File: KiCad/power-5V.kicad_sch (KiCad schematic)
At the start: 8 parts, among them U1 TPSM63606RDLR

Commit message: feat(pcb): add output capacitors
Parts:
- added C5, C6: (no value), symbol GCM32ER70J476KE19L:GCM32ER70J476KE19L
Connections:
- net GNDREF: now also C5.1, C6.1
- net VCC5: now also C5.2, C6.2
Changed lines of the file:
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@@
   (junction (at 116.84 83.82) (diameter 0) (color 0 0 0 0)
   )
-  (junction (at 177.8 111.76) (diameter 0) (color 0 0 0 0)
+  (junction (at 195.58 129.54) (diameter 0) (color 0 0 0 0)
+  )
+  (junction (at 185.42 111.76) (diameter 0) (color 0 0 0 0)
   )
   (junction (at 104.14 129.54) (diameter 0) (color 0 0 0 0)
@@
   (junction (at 128.27 129.54) (diameter 0) (color 0 0 0 0)
   )
+  (junction (at 219.71 129.54) (diameter 0) (color 0 0 0 0)
+  )
   (junction (at 177.8 129.54) (diameter 0) (color 0 0 0 0)
   )
@@
   (junction (at 180.34 83.82) (diameter 0) (color 0 0 0 0)
   )
+  (junction (at 219.71 83.82) (diameter 0) (color 0 0 0 0)
+  )
   (junction (at 195.58 107.95) (diameter 0) (color 0 0 0 0)
   )
@@
   (junction (at 177.8 121.92) (diameter 0) (color 0 0 0 0)
   )
+  (junction (at 232.41 83.82) (diameter 0) (color 0 0 0 0)
+  )
+  (no_connect (at 177.8 104.14))
   (no_connect (at 134.62 121.92))
   (no_connect (at 134.62 106.68))
   (no_connect (at 134.62 111.76))
-  (no_connect (at 177.8 104.14))
   (wire (pts (xy 104.14 81.28) (xy 104.14 83.82))
     (stroke (width 0) (type default) (color 0 0 0 0))
@@
     (stroke (width 0) (type default) (color 0 0 0 0))
   )
-  (wire (pts (xy 177.8 111.76) (xy 181.61 111.76))
-    (stroke (width 0) (type default) (color 0 0 0 0))
-  )
   (wire (pts (xy 207.01 107.95) (xy 195.58 107.95))
     (stroke (width 0) (type default) (color 0 0 0 0))
@@
     (stroke (width 0) (type default) (color 0 0 0 0))
   )
+  (wire (pts (xy 219.71 88.9) (xy 219.71 83.82))
+    (stroke (width 0) (type default) (color 0 0 0 0))
+  )
   (wire (pts (xy 177.8 81.28) (xy 180.34 81.28))
     (stroke (width 0) (type default) (color 0 0 0 0))
@@
     (stroke (width 0) (type default) (color 0 0 0 0))
   )
-  (wire (pts (xy 177.8 109.22) (xy 177.8 111.76))
-    (stroke (width 0) (type default) (color 0 0 0 0))
-  )
   (wire (pts (xy 186.69 105.41) (xy 195.58 105.41))
     (stroke (width 0) (type default) (color 0 0 0 0))
@@
     (stroke (width 0) (type default) (color 0 0 0 0))
   )
+  (wire (pts (xy 185.42 109.22) (xy 185.42 111.76))
+    (stroke (width 0) (type default) (color 0 0 0 0))
+  )
   (wire (pts (xy 180.34 81.28) (xy 180.34 83.82))
     (stroke (width 0) (type default) (color 0 0 0 0))
@@
     (stroke (width 0) (type default) (color 0 0 0 0))
   )
+  (wire (pts (xy 185.42 111.76) (xy 185.42 115.57))
+    (stroke (width 0) (type default) (color 0 0 0 0))
+  )
   (wire (pts (xy 207.01 83.82) (xy 207.01 88.9))
     (stroke (width 0) (type default) (color 0 0 0 0))
   )
+  (wire (pts (xy 232.41 88.9) (xy 232.41 83.82))
+    (stroke (width 0) (type default) (color 0 0 0 0))
+  )
   (wire (pts (xy 116.84 83.82) (xy 116.84 86.36))
     (stroke (width 0) (type default) (color 0 0 0 0))
@@
     (stroke (width 0) (type default) (color 0 0 0 0))
   )
+  (wire (pts (xy 177.8 109.22) (xy 185.42 109.22))
+    (stroke (width 0) (type default) (color 0 0 0 0))
+  )
+  (wire (pts (xy 232.41 101.6) (xy 232.41 129.54))
+    (stroke (width 0) (type default) (color 0 0 0 0))
+  )
   (wire (pts (xy 195.58 105.41) (xy 195.58 107.95))
     (stroke (width 0) (type default) (color 0 0 0 0))
   )
+  (wire (pts (xy 219.71 101.6) (xy 219.71 129.54))
+    (stroke (width 0) (type default) (color 0 0 0 0))
+  )
   (wire (pts (xy 177.8 119.38) (xy 177.8 121.92))
     (stroke (width 0) (type default) (color 0 0 0 0))
@@
     (stroke (width 0) (type default) (color 0 0 0 0))
   )
+  (wire (pts (xy 219.71 83.82) (xy 232.41 83.82))
+    (stroke (width 0) (type default) (color 0 0 0 0))
+  )
   (wire (pts (xy 129.54 101.6) (xy 119.38 101.6))
     (stroke (width 0) (type default) (color 0 0 0 0))
@@
     (stroke (width 0) (type default) (color 0 0 0 0))
   )
+  (wire (pts (xy 232.41 83.82) (xy 237.49 83.82))
+    (stroke (width 0) (type default) (color 0 0 0 0))
+  )
   (wire (pts (xy 129.54 101.6) (xy 129.54 67.31))
     (stroke (width 0) (type default) (color 0 0 0 0))
@@
     (stroke (width 0) (type default) (color 0 0 0 0))
   )
-  (wire (pts (xy 207.01 83.82) (xy 220.98 83.82))
+  (wire (pts (xy 207.01 83.82) (xy 219.71 83.82))
     (stroke (width 0) (type default) (color 0 0 0 0))
   )
@@
     (stroke (width 0) (type default) (color 0 0 0 0))
   )
+  (wire (pts (xy 177.8 111.76) (xy 185.42 111.76))
+    (stroke (width 0) (type default) (color 0 0 0 0))
+  )
+  (wire (pts (xy 232.41 129.54) (xy 219.71 129.54))
+    (stroke (width 0) (type default) (color 0 0 0 0))
+  )
+  (wire (pts (xy 219.71 129.54) (xy 195.58 129.54))
+    (stroke (width 0) (type default) (color 0 0 0 0))
+  )
   (wire (pts (xy 119.38 127) (xy 119.38 129.54))
     (stroke (width 0) (type default) (color 0 0 0 0))
@@
     (stroke (width 0) (type default) (color 0 0 0 0))
   )
-  (global_label "VCC5" (shape output) (at 220.98 83.82 0) (fields_autoplaced)
+  (global_label "VCC5" (shape output) (at 237.49 83.82 0) (fields_autoplaced)
     (effects (font (size 1.27 1.27)) (justify left))
-    (property "Intersheet References" "${INTERSHEET_REFS}" (id 0) (at 228.2312 83.7406 0)
+    (property "Intersheet References" "${INTERSHEET_REFS}" (id 0) (at 244.7412 83.7406 0)
       (effects (font (size 1.27 1.27)) (justify left) hide)
     )
@@
     (pin "2")
   )
+  (symbol (lib_id "GCM32ER70J476KE19L:GCM32ER70J476KE19L") (at 232.41 101.6 90) (unit 1)
+    (in_bom yes) (on_board yes) (fields_autoplaced)
+    (property "Reference" "C6" (id 0) (at 236.22 93.9799 90)
+      (effects (font (size 1.27 1.27)) (justify right))
+    )
+    (property "Value" "" (id 1) (at 236.22 96.5199 90)
+      (effects (font (size 1.27 1.27)) (justify right))
+    )
+    (property "Footprint" "" (id 2) (at 231.14 92.71 0)
+      (effects (font (size 1.27 1.27)) (justify left) hide)
+    )
+    (property "Datasheet" "" (id 3) (at 233.68 92.71 0)
+      (effects (font (size 1.27 1.27)) (justify left) hide)
+    )
+    (property "Description" "Chip Multilayer Ceramic Capacitors for Automotive" (id 4) (at 236.22 92.71 0)
+      (effects (font (size 1.27 1.27)) (justify left) hide)
+    )
+    (property "Height" "2.7" (id 5) (at 238.76 92.71 0)
+      (effects (font (size 1.27 1.27)) (justify left) hide)
+    )
+    (property "Mouser Part Number" "81-GCM32ER70J476KE9L" (id 6) (at 241.3 92.71 0)
+      (effects (font (size 1.27 1.27)) (justify left) hide)
+    )
+    (property "Mouser Price/Stock" "https://www.mouser.co.uk/ProductDetail/Murata-Electronics/GCM32ER70J476KE19L?qs=pIXLFAqUTcbyFoZMTWAW5w%3D%3D" (id 7) (at 243.84 92.71 0)
+      (effects (font (size 1.27 1.27)) (justify left) hide)
+    )
+    (property "Manufacturer_Name" "Murata Electronics" (id 8) (at 246.38 92.71 0)
+      (effects (font (size 1.27 1.27)) (justify left) hide)
+    )
+    (property "Manufacturer_Part_Number" "GCM32ER70J476KE19L" (id 9) (at 248.92 92.71 0)
+      (effects (font (size 1.27 1.27)) (justify left) hide)
+    )
+    (pin "1")
+    (pin "2")
+  )
   (symbol (lib_id "CRCW040210K0FKED:CRCW040210K0FKED") (at 195.58 127 90) (unit 1)
     (in_bom yes) (on_board yes) (fields_autoplaced)
@@
     (pin "1")
   )
-  (symbol (lib_id "power:GND") (at 181.61 111.76 90) (unit 1)
-    (in_bom yes) (on_board yes) (fields_autoplaced)
-    (property "Reference" "#PWR0104" (id 0) (at 187.96 111.76 0)
-      (effects (font (size 1.27 1.27)) hide)
-    )
-    (property "Value" "" (id 1) (at 185.42 111.7599 90)
-      (effects (font (size 1.27 1.27)) (justify right))
-    )
-    (property "Footprint" "" (id 2) (at 181.61 111.76 0)
-      (effects (font (size 1.27 1.27)) hide)
-    )
-    (property "Datasheet" "" (id 3) (at 181.61 111.76 0)
+  (symbol (lib_id "power:GND") (at 185.42 115.57 0) (unit 1)
+    (in_bom yes) (on_board yes) (fields_autoplaced)
+    (property "Reference" "#PWR0104" (id 0) (at 185.42 121.92 0)
+      (effects (font (size 1.27 1.27)) hide)
+    )
+    (property "Value" "" (id 1) (at 185.42 120.65 0))
+    (property "Footprint" "" (id 2) (at 185.42 115.57 0)
+      (effects (font (size 1.27 1.27)) hide)
+    )
+    (property "Datasheet" "" (id 3) (at 185.42 115.57 0)
       (effects (font (size 1.27 1.27)) hide)
     )
@@
       (effects (font (size 1.27 1.27)) (justify left) hide)
     )
+    (pin "1")
+    (pin "2")
+  )
+  (symbol (lib_id "GCM32ER70J476KE19L:GCM32ER70J476KE19L") (at 219.71 101.6 90) (unit 1)
+    (in_bom yes) (on_board yes) (fields_autoplaced)
+    (property "Reference" "C5" (id 0) (at 223.52 93.9799 90)
+      (effects (font (size 1.27 1.27)) (justify right))
+    )
+    (property "Value" "" (id 1) (at 223.52 96.5199 90)
+      (effects (font (size 1.27 1.27)) (justify right))
+    )
+    (property "Footprint" "" (id 2) (at 218.44 92.71 0)
+      (effects (font (size 1.27 1.27)) (justify left) hide)
+    )
+    (property "Datasheet" "" (id 3) (at 220.98 92.71 0)
+      (effects (font (size 1.27 1.27)) (justify left) hide)
+    )
+    (property "Description" "Chip Multilayer Ceramic Capacitors for Automotive" (id 4) (at 223.52 92.71 0)
+      (effects (font (size 1.27 1.27)) (justify left) hide)
+    )
+    (property "Height" "2.7" (id 5) (at 226.06 92.71 0)
+      (effects (font (size 1.27 1.27)) (justify left) hide)
+    )
+    (property "Mouser Part Number" "81-GCM32ER70J476KE9L" (id 6) (at 228.6 92.71 0)
+      (effects (font (size 1.27 1.27)) (justify left) hide)
+    )
+    (property "Mouser Price/Stock" "https://www.mouser.co.uk/ProductDetail/Murata-Electronics/GCM32ER70J476KE19L?qs=pIXLFAqUTcbyFoZMTWAW5w%3D%3D" (id 7) (at 231.14 92.71 0)
+      (effects (font (size 1.27 1.27)) (justify left) hide)
+    )
+    (property "Manufacturer_Name" "Murata Electronics" (id 8) (at 233.68 92.71 0)
+      (effects (font (size 1.27 1.27)) (justify left) hide)
+    )
+    (property "Manufacturer_Part_Number" "GCM32ER70J476KE19L" (id 9) (at 236.22 92.71 0)
+      (effects (font (size 1.27 1.27)) (justify left) hide)
+    )

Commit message: feat(pcb): add footprints
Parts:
- C1, C2: value (none) -> 10uF
- C3: value (none) -> 1uF
- C4: value (none) -> 8.2pF
- C5, C6: value (none) -> 47uF
- R1: value (none) -> 12.1k; footprint (none) -> Resistor_SMD:R_0402_1005Metric
- R2: value (none) -> 40.2k
- R3: value (none) -> 10k
- U1: footprint RDL0020A-MFG -> (none)
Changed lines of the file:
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@@
       (effects (font (size 1.27 1.27)) (justify left))
     )
-    (property "Value" "" (id 1) (at 130.81 124.4599 0)
+    (property "Value" "12.1k" (id 1) (at 130.81 124.4599 0)
       (effects (font (size 1.27 1.27)) (justify left))
     )
-    (property "Footprint" "" (id 2) (at 126.492 123.19 90)
+    (property "Footprint" "Resistor_SMD:R_0402_1005Metric" (id 2) (at 126.492 123.19 90)
       (effects (font (size 1.27 1.27)) hide)
     )
@@
       (effects (font (size 1.27 1.27)) hide)
     )
-    (property "Value" "" (id 1) (at 104.14 135.89 0))
+    (property "Value" "GNDREF" (id 1) (at 104.14 135.89 0))
     (property "Footprint" "" (id 2) (at 104.14 130.81 0)
       (effects (font (size 1.27 1.27)) hide)
@@
       (effects (font (size 1.27 1.27)) (justify right))
     )
-    (property "Value" "" (id 1) (at 120.65 93.9799 90)
+    (property "Value" "10uF" (id 1) (at 120.65 93.9799 90)
       (effects (font (size 1.27 1.27)) (justify right))
     )
@@
       (effects (font (size 1.27 1.27)) (justify right))
     )
-    (property "Value" "" (id 1) (at 123.19 121.9199 90)
+    (property "Value" "1uF" (id 1) (at 123.19 121.9199 90)
       (effects (font (size 1.27 1.27)) (justify right))
     )
@@
       (effects (font (size 1.27 1.27)) (justify right))
     )
-    (property "Value" "" (id 1) (at 236.22 96.5199 90)
+    (property "Value" "47uF" (id 1) (at 236.22 96.5199 90)
       (effects (font (size 1.27 1.27)) (justify right))
     )
@@
       (effects (font (size 1.27 1.27)) (justify right))
     )
-    (property "Value" "" (id 1) (at 198.12 119.3799 90)
+    (property "Value" "10k" (id 1) (at 198.12 119.3799 90)
       (effects (font (size 1.27 1.27)) (justify right))
     )
@@
       (effects (font (size 1.27 1.27)) (justify right))
     )
-    (property "Value" "" (id 1) (at 210.82 96.5199 90)
+    (property "Value" "8.2pF" (id 1) (at 210.82 96.5199 90)
       (effects (font (size 1.27 1.27)) (justify right))
     )
@@
       (effects (font (size 1.27 1.27)) (justify right))
     )
-    (property "Value" "" (id 1) (at 198.12 96.5199 90)
+    (property "Value" "40.2k" (id 1) (at 198.12 96.5199 90)
       (effects (font (size 1.27 1.27)) (justify right))
     )
@@
       (effects (font (size 1.27 1.27)) hide)
     )
-    (property "Value" "" (id 1) (at 104.14 76.2 0))
+    (property "Value" "+BATT" (id 1) (at 104.14 76.2 0))
     (property "Footprint" "" (id 2) (at 104.14 81.28 0)
       (effects (font (size 1.27 1.27)) hide)
@@
       (effects (font (size 1.27 1.27)) hide)
     )
-    (property "Value" "" (id 1) (at 185.42 120.65 0))
+    (property "Value" "GND" (id 1) (at 185.42 120.65 0))
     (property "Footprint" "" (id 2) (at 185.42 115.57 0)
       (effects (font (size 1.27 1.27)) hide)
@@
       (effects (font (size 1.524 1.524)))
     )
-    (property "Footprint" "RDL0020A-MFG" (id 2) (at 134.62 82.804 0)
+    (property "Footprint" "" (id 2) (at 134.62 82.804 0)
       (effects (font (size 1.524 1.524)) hide)
     )
@@
       (effects (font (size 1.27 1.27)) (justify right))
     )
-    (property "Value" "" (id 1) (at 107.95 93.9799 90)
+    (property "Value" "10uF" (id 1) (at 107.95 93.9799 90)
       (effects (font (size 1.27 1.27)) (justify right))
     )
@@
       (effects (font (size 1.27 1.27)) (justify right))
     )
-    (property "Value" "" (id 1) (at 223.52 96.5199 90)
-      (effects (font (size 1.27 1.27)) (justify right))
-    )
+    (property "Value" "47uF" (id 1) (at 223.52 96.5199 90)
+      (effects (font (size 1.27 1.27)) (justify right))
+    )

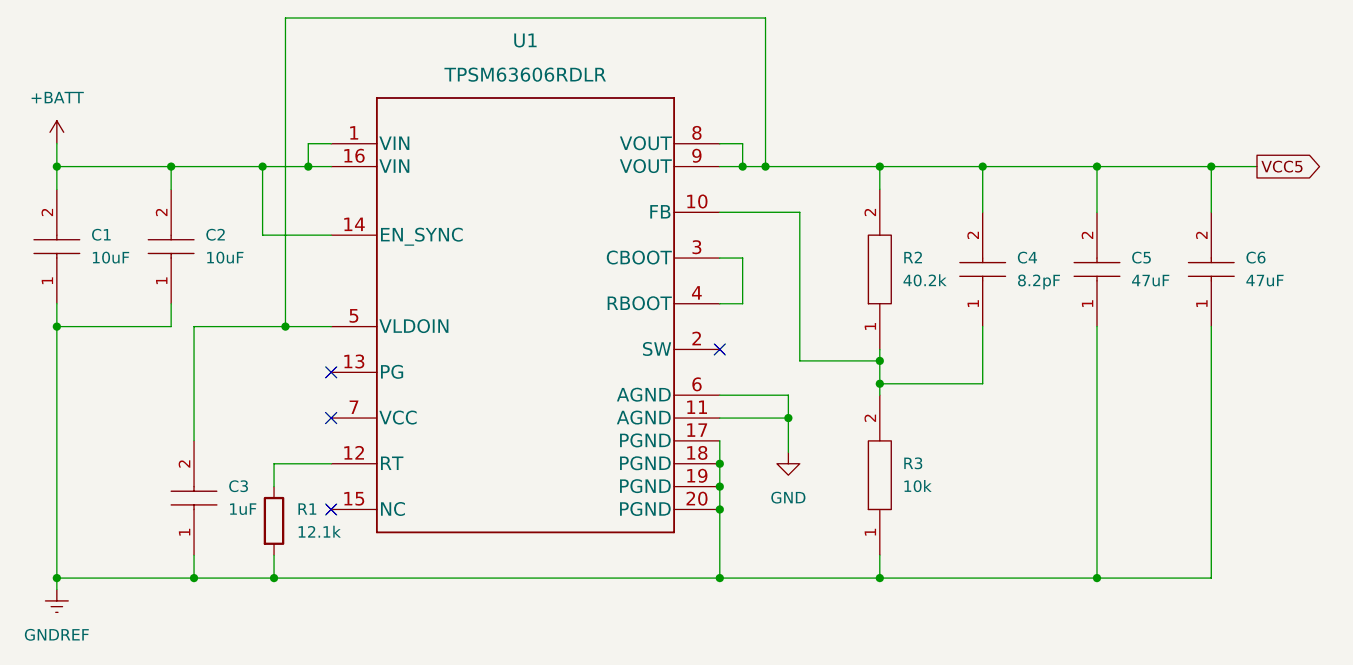
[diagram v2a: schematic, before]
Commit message: feat(pcb): add mounting holes
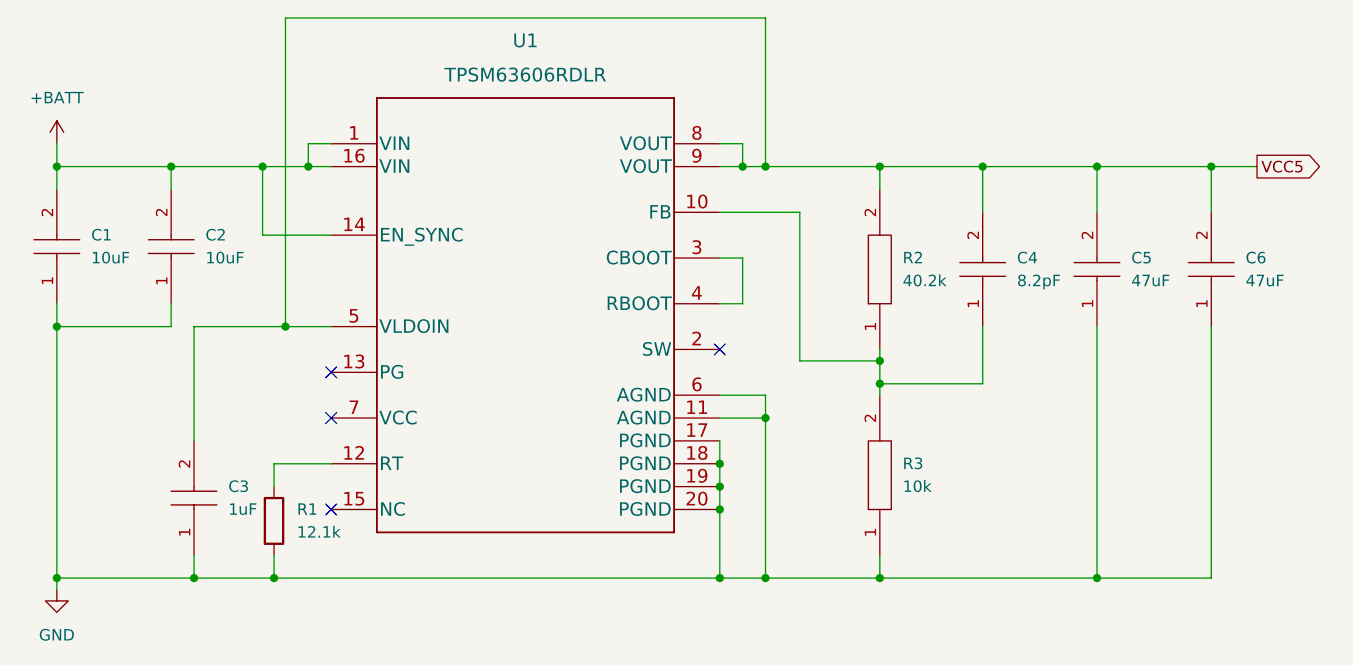
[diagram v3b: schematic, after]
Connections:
- net GNDREF is gone; now on net GND: C1.1, C2.1, C3.1, C5.1, C6.1, R1.2, R3.1, U1.17 (PGND), U1.18 (PGND), U1.19 (PGND), U1.20 (PGND)

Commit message: feat(pcb): add schematic for connectors
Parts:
- C1, C2: footprint (none) -> C3225X7R1H106M250AC:C3225_Commercial
- C3: footprint (none) -> C1005X6S1C105K050BC:C1005_Commercial
- C4: footprint (none) -> GRM1555C1H8R2CA01D:CAPC1005X55N
- C5, C6: footprint (none) -> GCM32ER70J476KE19L:CAPC3225X270N
- R2, R3: footprint (none) -> CRCW040210K0FKED:RESC1005X40N
- U1: footprint (none) -> Power module:RDL0020A-MFG
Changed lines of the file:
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@@
       (effects (font (size 1.27 1.27)) (justify right))
     )
-    (property "Footprint" "" (id 2) (at 115.57 90.17 0)
+    (property "Footprint" "C3225X7R1H106M250AC:C3225_Commercial" (id 2) (at 115.57 90.17 0)
       (effects (font (size 1.27 1.27)) (justify left) hide)
     )
@@
       (effects (font (size 1.27 1.27)) (justify right))
     )
-    (property "Footprint" "" (id 2) (at 118.11 118.11 0)
+    (property "Footprint" "C1005X6S1C105K050BC:C1005_Commercial" (id 2) (at 118.11 118.11 0)
       (effects (font (size 1.27 1.27)) (justify left) hide)
     )
@@
       (effects (font (size 1.27 1.27)) (justify right))
     )
-    (property "Footprint" "" (id 2) (at 231.14 92.71 0)
+    (property "Footprint" "GCM32ER70J476KE19L:CAPC3225X270N" (id 2) (at 231.14 92.71 0)
       (effects (font (size 1.27 1.27)) (justify left) hide)
     )
@@
       (effects (font (size 1.27 1.27)) (justify right))
     )
-    (property "Footprint" "" (id 2) (at 194.31 113.03 0)
+    (property "Footprint" "CRCW040210K0FKED:RESC1005X40N" (id 2) (at 194.31 113.03 0)
       (effects (font (size 1.27 1.27)) (justify left) hide)
     )
@@
       (effects (font (size 1.27 1.27)) (justify right))
     )
-    (property "Footprint" "" (id 2) (at 205.74 92.71 0)
+    (property "Footprint" "GRM1555C1H8R2CA01D:CAPC1005X55N" (id 2) (at 205.74 92.71 0)
       (effects (font (size 1.27 1.27)) (justify left) hide)
     )
@@
       (effects (font (size 1.27 1.27)) (justify right))
     )
-    (property "Footprint" "" (id 2) (at 194.31 90.17 0)
+    (property "Footprint" "CRCW040210K0FKED:RESC1005X40N" (id 2) (at 194.31 90.17 0)
       (effects (font (size 1.27 1.27)) (justify left) hide)
     )
@@
       (effects (font (size 1.524 1.524)))
     )
-    (property "Footprint" "" (id 2) (at 134.62 82.804 0)
+    (property "Footprint" "Power module:RDL0020A-MFG" (id 2) (at 134.62 82.804 0)
       (effects (font (size 1.524 1.524)) hide)
     )
@@
       (effects (font (size 1.27 1.27)) (justify right))
     )
-    (property "Footprint" "" (id 2) (at 102.87 90.17 0)
+    (property "Footprint" "C3225X7R1H106M250AC:C3225_Commercial" (id 2) (at 102.87 90.17 0)
       (effects (font (size 1.27 1.27)) (justify left) hide)
     )
@@
       (effects (font (size 1.27 1.27)) (justify right))
     )
-    (property "Footprint" "" (id 2) (at 218.44 92.71 0)
-      (effects (font (size 1.27 1.27)) (justify left) hide)
-    )
+    (property "Footprint" "GCM32ER70J476KE19L:CAPC3225X270N" (id 2) (at 218.44 92.71 0)
+      (effects (font (size 1.27 1.27)) (justify left) hide)
+    )
